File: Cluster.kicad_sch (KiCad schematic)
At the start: 26 parts, among them J1 DTM06-2S nickel, 12V input (s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, J2 SWD Tag-Connect, Q1 PMV37ENEA automotive (AEC-Q10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, U1 NXP S32K144 automotive (AEC-Q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, U2 LMR33630-Q1 (AEC-Q100 G1), U3 LM74700-Q1 (AEC-Q100 G1), U4 TLV733P-Q1 (AEC-Q100 G1), Y1 8MHz (AEC-Q200)

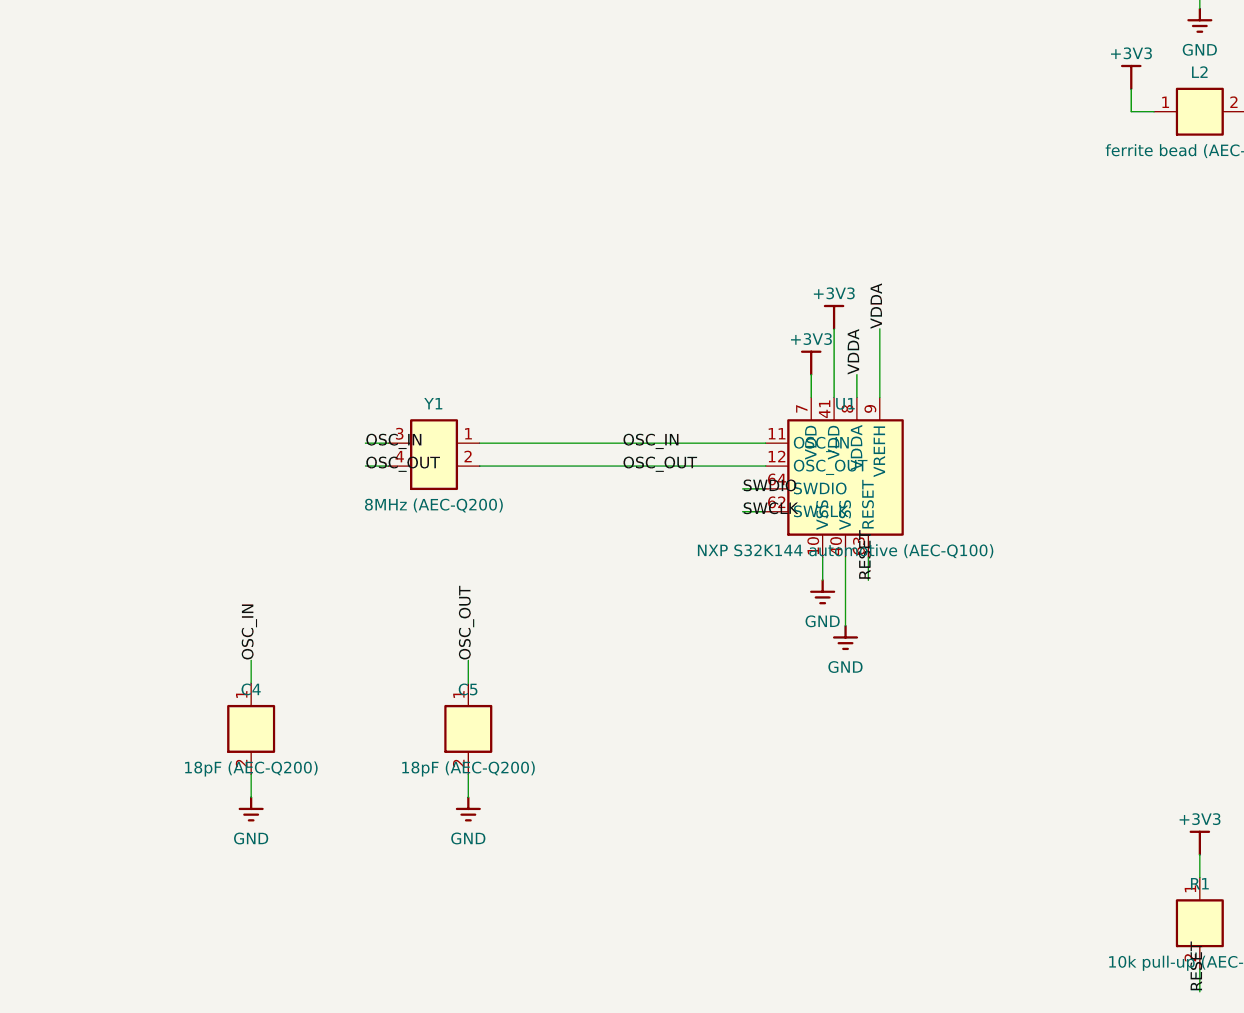
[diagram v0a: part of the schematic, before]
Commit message: Step 1: real S32K144 peripheral pin-mux for BT817AQ/aux gauges/CAN/ADC
Pulled the real IO signal table from NXP's own S32K1xx Reference Manual
(embedded xlsx attachment, extracted via pypdf) and picked 25
conflict-checked pins for LPSPI1 (BT817AQ QSPI), LPSPI2 (shared aux
gauge SPI bus), FlexCAN0, 4x ADC channel, and 9 plain GPIO. Wired as
real, named label stubs on U1 - not yet connected to any peripheral
chip, that's Steps 2-5. Regenerates clean; ERC shows only the expected
forward-stub findings.

Co-Authored-By: Claude Sonnet 5 <noreply@anthropic.com>
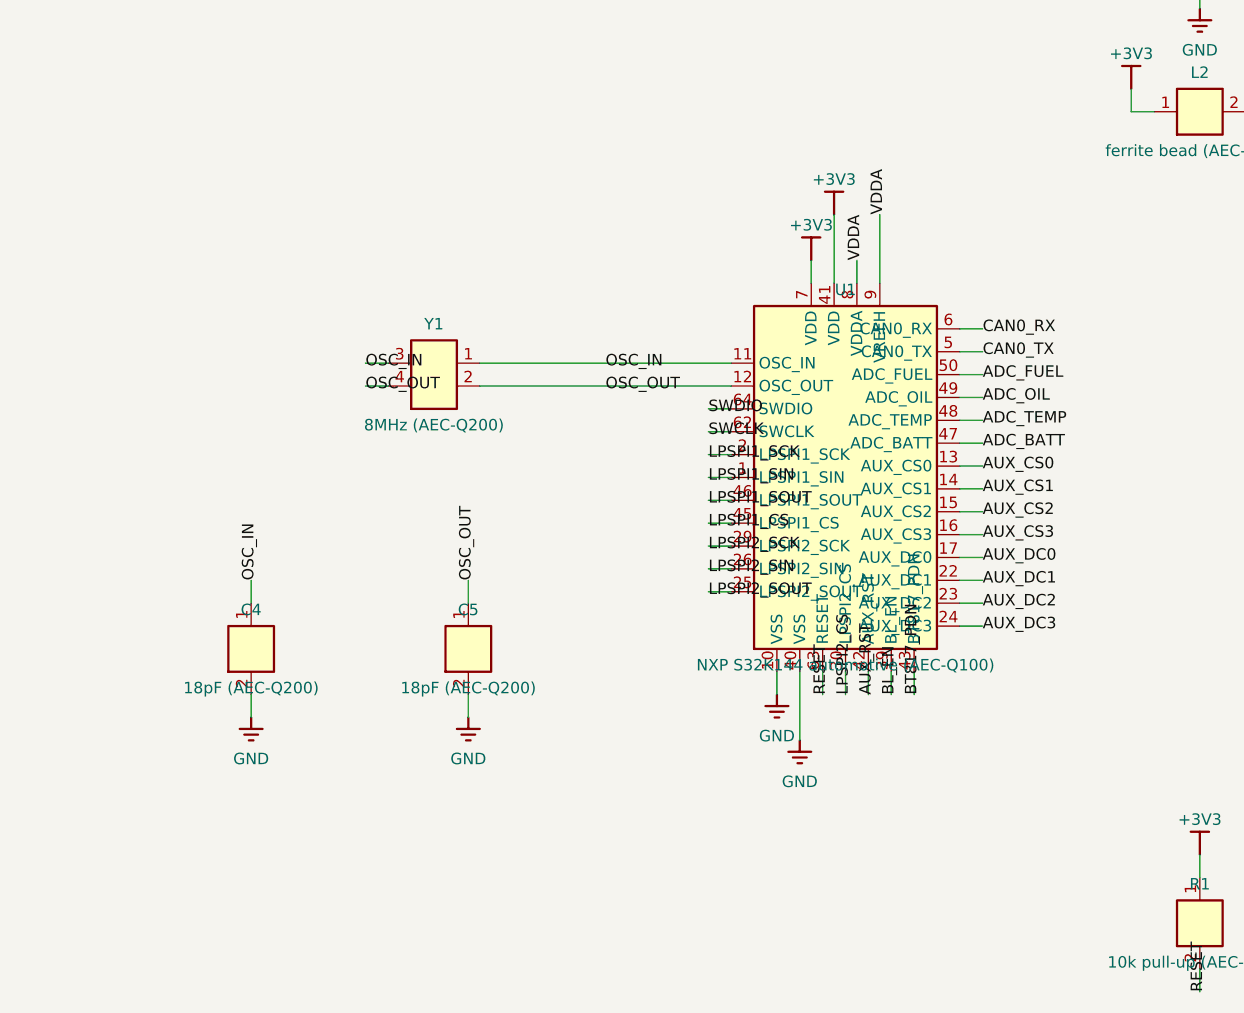
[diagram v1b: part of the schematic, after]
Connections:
- new net ADC_BATT: U1.47 (ADC_BATT)
- new net ADC_FUEL: U1.50 (ADC_FUEL)
- new net ADC_OIL: U1.49 (ADC_OIL)
- new net ADC_TEMP: U1.48 (ADC_TEMP)
- new net AUX_CS0: U1.13 (AUX_CS0)
- new net AUX_CS1: U1.14 (AUX_CS1)
- new net AUX_CS2: U1.15 (AUX_CS2)
- new net AUX_CS3: U1.16 (AUX_CS3)
- new net AUX_DC0: U1.17 (AUX_DC0)
- new net AUX_DC1: U1.22 (AUX_DC1)
- new net AUX_DC2: U1.23 (AUX_DC2)
- new net AUX_DC3: U1.24 (AUX_DC3)
- new net AUX_RST: U1.42 (AUX_RST)
- new net BL_EN: U1.39 (BL_EN)
- new net BT817_PDN: U1.43 (BT817_PDN)
- new net CAN0_RX: U1.6 (CAN0_RX)
- new net CAN0_TX: U1.5 (CAN0_TX)
- new net LPSPI1_CS: U1.45 (LPSPI1_CS)
- new net LPSPI1_SCK: U1.2 (LPSPI1_SCK)
- new net LPSPI1_SIN: U1.1 (LPSPI1_SIN)
- new net LPSPI1_SOUT: U1.46 (LPSPI1_SOUT)
- new net LPSPI2_CS: U1.30 (LPSPI2_CS)
- new net LPSPI2_SCK: U1.29 (LPSPI2_SCK)
- new net LPSPI2_SIN: U1.26 (LPSPI2_SIN)
- new net LPSPI2_SOUT: U1.25 (LPSPI2_SOUT)

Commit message: Steps 2-3: CAN0 transceiver + 4x GC9A01 aux gauges wired
Step 2: reused ecu-pcb's real, already-verified TJA1043T CAN transceiver
pin table and wiring topology verbatim (single CAN0 instance).

Step 3: registered the real 18-pin FPC table from Raystar's own
RFA401280B-AYW-DNF1 datasheet for the 4x GC9A01 aux gauges. Real finding
from reading the datasheet rather than assuming a generic GC9A01
breakout: backlight is a bare LED anode/cathode pair, not a logic-level
enable pin - wired with per-display series resistors from +5V and a
shared low-side MOSFET switch (reusing the power stage's own PMV37ENEA),
not 4 GPIO-driven logic pins.

Two real bugs caught and fixed by the script's own checks, not eyeballed:
a GND-riser-style collision between VCI3V3's power symbol and an
adjacent pin's stub, and a guessed FFC-FPC footprint name that doesn't
exist in KiCad's bundled library (fixed with a real bundled Amphenol
part). Grew the sheet from A2 to A1 for room. ERC clean except findings
that trace to Steps 4-5, not yet wired.

Co-Authored-By: Claude Sonnet 5 <noreply@anthropic.com>
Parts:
- added C13: 100nF VCC decouple (AEC-Q200), Capacitor_SMD:C_0603_1608Metric, symbol Cluster:C_V
- added C14: 100nF VIO decouple (AEC-Q200), Capacitor_SMD:C_0603_1608Metric, symbol Cluster:C_V
- added C15: 100nF VBAT decouple (AEC-Q200), Capacitor_SMD:C_0603_1608Metric, symbol Cluster:C_V
- added C16: 4.7nF SPLIT stabilization (AEC-Q200), Capacitor_SMD:C_0603_1608Metric, symbol Cluster:C_V
- added C17, C18, C19, C20: 100nF VCI decouple (AEC-Q200), Capacitor_SMD:C_0603_1608Metric, symbol Cluster:C_V
- added Q2: PMV37ENEA automotive (AEC-Q101) - shared aux-gaug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, Package_TO_SOT_SMD:SOT-23, symbol Cluster:MOSFET_N
- added R10: 100R BL_EN gate resistor (AEC-Q200), Resistor_SMD:R_0603_1608Metric, symbol Cluster:R_V
- added R11: 10k LPSPI2_SIN pull-down, idle-state definition (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, Resistor_SMD:R_0603_1608Metric, symbol Cluster:R_V
- added R4, R5: 60R split termination (AEC-Q200) - DNP unless bus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, Resistor_SMD:R_0603_1608Metric, symbol Cluster:R_V
- added R6, R7, R8, R9: 120R VLED series (self-calculated for ~15mA at 5V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, Resistor_SMD:R_0603_1608Metric, symbol Cluster:R_V
- added U5: NXP TJA1043T automotive CAN transceiver (AEC-Q100), Package_SO:SOIC-14_3.9x8.7mm_P1.27mm, symbol Cluster:TJA1043T
- added U6: Raystar RFA401280B-AYW-DNF1 - Fuel level gauge, Connector_FFC-FPC:Amphenol_F32Q-1A7x1-11018_1x18-1MP_P0.5mm_Horizontal, symbol Cluster:GC9A01_MODULE
- added U7: Raystar RFA401280B-AYW-DNF1 - Oil pressure gauge, Connector_FFC-FPC:Amphenol_F32Q-1A7x1-11018_1x18-1MP_P0.5mm_Horizontal, symbol Cluster:GC9A01_MODULE
- added U8: Raystar RFA401280B-AYW-DNF1 - Coolant temp gauge, Connector_FFC-FPC:Amphenol_F32Q-1A7x1-11018_1x18-1MP_P0.5mm_Horizontal, symbol Cluster:GC9A01_MODULE
- added U9: Raystar RFA401280B-AYW-DNF1 - Battery voltage gau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, Connector_FFC-FPC:Amphenol_F32Q-1A7x1-11018_1x18-1MP_P0.5mm_Horizontal, symbol Cluster:GC9A01_MODULE
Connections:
- net +3V3: now also C14.1, C17.1, C18.1, C19.1, C20.1, U5.5 (VIO), U6.16 (VCI3V3), U7.16 (VCI3V3), U8.16 (VCI3V3), U9.16 (VCI3V3)
- net +5V: now also C13.1, R6.1, R7.1, R8.1, R9.1, U5.3 (VCC)
- net AUX_CS0: now also U6.10 (CS)
- net AUX_CS1: now also U7.10 (CS)
- net AUX_CS2: now also U8.10 (CS)
- net AUX_CS3: now also U9.10 (CS)
- net AUX_DC0: now also U6.13 (RS)
- net AUX_DC1: now also U7.13 (RS)
- net AUX_DC2: now also U8.13 (RS)
- net AUX_DC3: now also U9.13 (RS)
- net AUX_RST: now also U6.15 (RESET), U7.15 (RESET), U8.15 (RESET), U9.15 (RESET)
- net BL_EN: now also R10.1
- net CAN0_RX: now also U5.4 (RXD)
- net CAN0_TX: now also U5.1 (TXD)
- net GND: now also C13.2, C14.2, C15.2, C16.2, C17.2, C18.2, C19.2, C20.2, Q2.3 (D), R11.2, U5.2 (GND), U5.9 (WAKE), U6.18 (GND), U6.5 (TP_GND), U6.9 (GND), U7.18 (GND), U7.5 (TP_GND), U7.9 (GND), U8.18 (GND), U8.5 (TP_GND), U8.9 (GND), U9.18 (GND), U9.5 (TP_GND), U9.9 (GND)
- net LPSPI2_SCK: now also U6.11 (SCL), U7.11 (SCL), U8.11 (SCL), U9.11 (SCL)
- net LPSPI2_SIN: now also R11.1
- net LPSPI2_SOUT: now also U6.12 (SDA), U7.12 (SDA), U8.12 (SDA), U9.12 (SDA)
- net VIN_PROT: now also C15.1, U5.10 (VBAT)
- net LPSPI2_CS: no longer names the net of U1.30 (LPSPI2_CS)
- new net AUX_VLED_RTN: Q2.2 (S), U6.8 (VLED-), U7.8 (VLED-), U8.8 (VLED-), U9.8 (VLED-)
- new net BL_GATE: Q2.1 (G), R10.2
- new net CAN0_EN: U1.18 (CAN0_EN), U5.6 (EN)
- new net CAN0_H: R4.1, U5.13 (CANH)
- new net CAN0_L: R5.2, U5.12 (CANL)
- new net CAN0_SPLIT: C16.1, R4.2, R5.1, U5.11 (SPLIT)
- new net CAN0_STB_N: U1.19 (CAN0_STB_N), U5.14 (STB_N)
- new net U6_VLED: R6.2, U6.7 (VLED+)
- new net U7_VLED: R7.2, U7.7 (VLED+)
- new net U8_VLED: R8.2, U8.7 (VLED+)
- new net U9_VLED: R9.2, U9.7 (VLED+)
- no-connect marks 3 -> 34
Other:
- note added: "4x GC9A01 AUX GAUGES: FUEL / OIL / COOLANT TEMP / BATTERY (PLAN STEP 3)"
- note added: "CAN0: NXP TJA1043T TRANSCEIVER (PLAN STEP 2)"

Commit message: Step 4: BT817AQ speedo co-processor + ST7701S module wired
Registered BT817AQ's real 64-pin VQFN table from Bridgetek's own
datasheet and the BH021WVC02 module's real 40-pin FPC table from
Panox's own datasheet. Real finding along the way: BT817A's VCC1V2
core rail is a genuine external 1.28V supply (not internally regulated
from VCC), so a new TPS7A16-Q1 adjustable LDO + FB divider was added,
sized from TI's own VREF spec. RGB666 wiring uses the module's own
documented bit order (DB0=Blue LSB..DB17=Red MSB) to map BT817AQ's
R7-R2/G7-G2/B7-B2 correctly. Speedo backlight reuses the same real
"series resistor + shared MOSFET switch" LED treatment as the aux
gauges, this time PWM-driven from BT817AQ's own BACKLIGHT output for
independent dimming.

Two real bugs caught and fixed, not eyeballed: a crystal-to-MCU wiring
attempt using wire_pins() across mismatched pin orientations (same
class of bug thermo-pcb's own history documents, fixed with label-based
connections instead), and a genuine placement collision between U10 and
Y2 that produced a real ERC pin_to_pin/multiple_net_names short -
confirmed via a rendered PDF crop showing the two symbols' pin fields
interleaved, fixed with real separation. ERC clean except findings that
trace to Step 5 (sensor ADC front end), not yet wired.

Co-Authored-By: Claude Sonnet 5 <noreply@anthropic.com>
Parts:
- added C21: 10uF IN cap (AEC-Q200), Capacitor_SMD:C_0603_1608Metric, symbol Cluster:C_V
- added C22: 10uF OUT cap, real min 2.2uF per TI's own stabili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, Capacitor_SMD:C_0603_1608Metric, symbol Cluster:C_V
- added C23, C24: 18pF (AEC-Q200), Capacitor_SMD:C_0603_1608Metric, symbol Cluster:C_V
- added C25: 100nF VCC decouple (AEC-Q200), Capacitor_SMD:C_0603_1608Metric, symbol Cluster:C_V
- added C26: 1uF VCC1V2 decouple (AEC-Q200), Capacitor_SMD:C_0603_1608Metric, symbol Cluster:C_V
- added C27: 100nF VCCIO decouple (AEC-Q200), Capacitor_SMD:C_0603_1608Metric, symbol Cluster:C_V
- added J3: Panox BH021WVC02 - center speedo, Connector_FFC-FPC:Amphenol_F32Q-1A7x1-11040_1x40-1MP_P0.5mm_Horizontal, symbol Cluster:ST7701S_MODULE
- added Q3: PMV37ENEA automotive (AEC-Q101) - speedo backligh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, Package_TO_SOT_SMD:SOT-23, symbol Cluster:MOSFET_N
- added R12: 7.32k FB divider top, self-calculated for 1.28V (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, Resistor_SMD:R_0603_1608Metric, symbol Cluster:R_V
- added R13: 100k FB divider bottom, self-calculated for 1.28V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, Resistor_SMD:R_0603_1608Metric, symbol Cluster:R_V
- added R14: 120R LEDA series (self-calculated, ~15mA at 5V - 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, Resistor_SMD:R_0603_1608Metric, symbol Cluster:R_V
- added R15: 100R SPD_BL_PWM gate resistor (AEC-Q200), Resistor_SMD:R_0603_1608Metric, symbol Cluster:R_V
- added U10: TPS7A16-Q1 (AEC-Q100 G1), Package_SO:Texas_DGN0008D_VSSOP-8-1EP_3x3mm_P0.65mm_EP2x2.94mm_Mask1.57x1.89mm, symbol Cluster:IC_LDO_ADJ
- added U11: Bridgetek BT817AQ automotive (AEC-Q100 G2), Package_DFN_QFN:QFN-64-1EP_9x9mm_P0.5mm_EP4.1x4.1mm, symbol Cluster:BT817AQ
- added Y2: 12MHz (AEC-Q200), Crystal:Crystal_SMD_3225-4Pin_3.2x2.5mm, symbol Cluster:XTAL_BT817
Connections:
- net +3V3: now also C21.1, C25.1, C27.1, J3.5 (VCI), U10.5 (EN), U10.8 (IN), U11.17 (VCCIO3), U11.24 (VCC), U11.27 (VCCA), U11.28 (VCCIO2), U11.9 (VCCIO1)
- net +5V: now also R14.1
- net BT817_PDN: now also U11.12 (PD_N)
- net GND: now also C21.2, C22.2, C23.2, C24.2, C25.2, C26.2, C27.2, J3.34 (GND), J3.4 (GND), J3.40 (GND), Q3.3 (D), R13.2, U10.4 (GND), U10.9 (EP), U11.18 (SPIM_MISO), U11.23 (GND), U11.33 (GND), U11.48 (GND), U11.65 (EP)
- net LPSPI1_CS: now also U11.6 (CS_N)
- net LPSPI1_SCK: now also U11.3 (SCK)
- net LPSPI1_SIN: now also U11.4 (MISO)
- net LPSPI1_SOUT: now also U11.5 (MOSI)
- new net BT817_X1: C23.1, U11.21 (X1), Y2.1 (X1), Y2.3 (X1)
- new net BT817_X2: C24.1, U11.22 (X2), Y2.2 (X2), Y2.4 (X2)
- new net DE: J3.13 (DE), U11.35 (DE)
- new net FB1V2: R12.2, R13.1, U10.2 (FB)
- new net HSYNC: J3.15 (HSYNC), U11.37 (HSYNC)
- new net J3_LEDA: J3.1 (LEDA), R14.2
- new net PCLK: J3.12 (PCLK), U11.39 (PCLK)
- new net SPD_B2: J3.16 (DB0), U11.45 (B2)
- new net SPD_B3: J3.17 (DB1), U11.44 (B3)
- new net SPD_B4: J3.18 (DB2), U11.43 (B4)
- new net SPD_B5: J3.19 (DB3), U11.42 (B5)
- new net SPD_B6: J3.20 (DB4), U11.41 (B6)
- new net SPD_B7: J3.21 (DB5), U11.40 (B7)
- new net SPD_BL_GATE: Q3.1 (G), R15.2
- new net SPD_BL_PWM: R15.1, U11.34 (BACKLIGHT)
- new net SPD_G2: J3.22 (DB6), U11.54 (G2)
- new net SPD_G3: J3.23 (DB7), U11.53 (G3)
- new net SPD_G4: J3.24 (DB8), U11.52 (G4)
- new net SPD_G5: J3.25 (DB9), U11.51 (G5)
- new net SPD_G6: J3.26 (DB10), U11.50 (G6)
- new net SPD_G7: J3.27 (DB11), U11.49 (G7)
- new net SPD_R2: J3.28 (DB12), U11.63 (R2)
- new net SPD_R3: J3.29 (DB13), U11.62 (R3)
- new net SPD_R4: J3.30 (DB14), U11.61 (R4)
- new net SPD_R5: J3.31 (DB15), U11.60 (R5)
- new net SPD_R6: J3.32 (DB16), U11.59 (R6)
- new net SPD_R7: J3.33 (DB17), U11.58 (R7)
- new net SPD_VLED_RTN: J3.2 (LEDK), J3.3 (LEDK), Q3.2 (S)
- new net ST7701_CS: J3.11 (CS), U11.10 (GPIO2)
- new net ST7701_RESET: J3.6 (RESET), U11.13 (GPIO3)
- new net ST7701_SCK: J3.10 (SCK), U11.8 (GPIO1)
- new net ST7701_SDA: J3.9 (SDA), U11.7 (GPIO0)
- new net VCC1V2: C22.1, C26.1, R12.1, U10.1 (OUT), U11.2 (VCC1V2), U11.25 (VCC1V2), U11.57 (VCC1V2)
- new net VSYNC: J3.14 (VSYNC), U11.36 (VSYNC)
- no-connect marks 34 -> 62
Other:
- note added: "BT817AQ + ST7701S SPEEDO MODULE (PLAN STEP 4)"

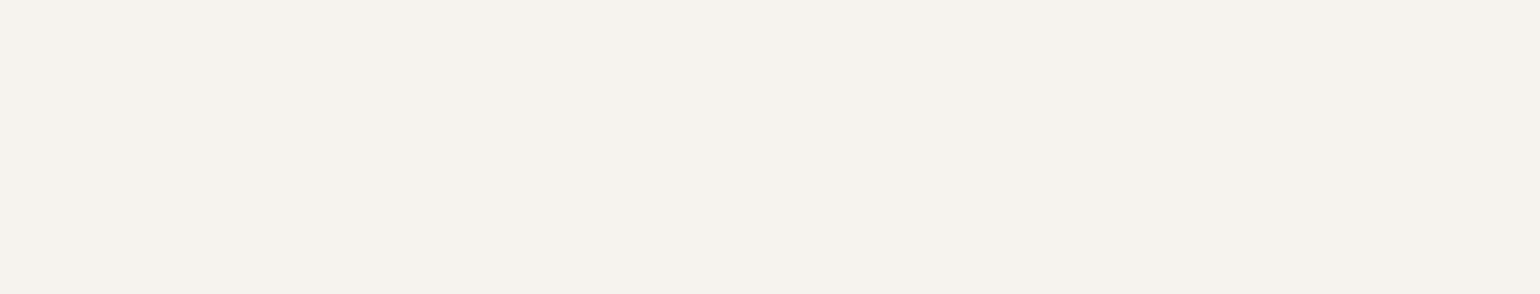
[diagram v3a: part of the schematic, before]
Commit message: Step 5: sensor ADC front end wired; schematic now fully wired
Fuel/oil/temp resistive dividers sized per-sender from the real
published curves (fuel/oil share a 47R pull-up given their similar
10-70ish-ohm range; coolant temp gets its own 100R pull-up for its much
wider 10-300R range). Battery voltage divider (49.9k/10k) scaled for
the real 9-16V automotive range with margin below the ADC's 3.3V rail.

ERC is down to exactly the 4 baseline findings every sibling board's
finished schematic carries (VDDA/U2-VIN/+5V power_pin_not_driven,
SWCLK driven off-sheet) - every real forward stub from Steps 1-5 is now
resolved except the genuine off-board harness connections pending Step
6. Also grew the sheet A1->A0: a full-page render (the same "always
verify with a real render" discipline this family's history keeps
re-learning) showed J3 genuinely clipped past A1's right edge.

Co-Authored-By: Claude Sonnet 5 <noreply@anthropic.com>
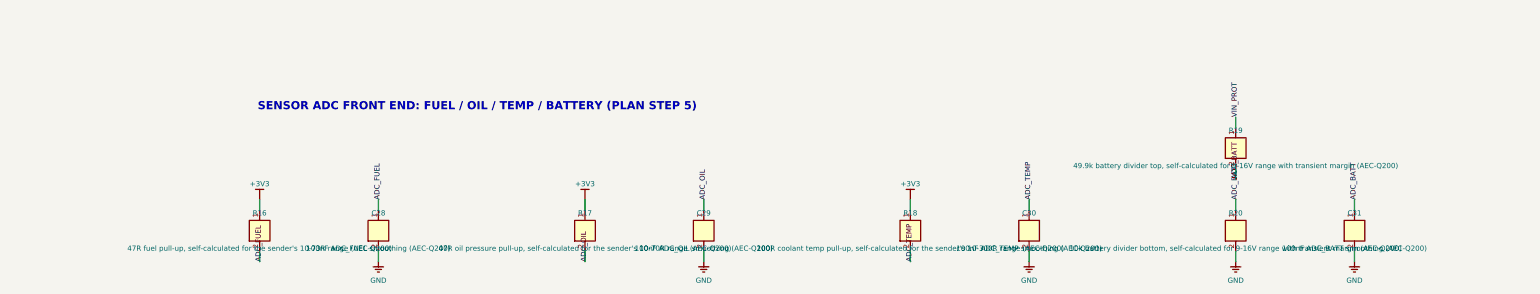
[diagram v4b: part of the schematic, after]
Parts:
- added C28: 100nF ADC_FUEL smoothing (AEC-Q200), Capacitor_SMD:C_0603_1608Metric, symbol Cluster:C_V
- added C29: 100nF ADC_OIL smoothing (AEC-Q200), Capacitor_SMD:C_0603_1608Metric, symbol Cluster:C_V
- added C30: 100nF ADC_TEMP smoothing (AEC-Q200), Capacitor_SMD:C_0603_1608Metric, symbol Cluster:C_V
- added C31: 100nF ADC_BATT smoothing (AEC-Q200), Capacitor_SMD:C_0603_1608Metric, symbol Cluster:C_V
- added R16: 47R fuel pull-up, self-calculated for the sender'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, Resistor_SMD:R_0603_1608Metric, symbol Cluster:R_V
- added R17: 47R oil pressure pull-up, self-calculated for the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, Resistor_SMD:R_0603_1608Metric, symbol Cluster:R_V
- added R18: 100R coolant temp pull-up, self-calculated for th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, Resistor_SMD:R_0603_1608Metric, symbol Cluster:R_V
- added R19: 49.9k battery divider top, self-calculated for 9-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, Resistor_SMD:R_0603_1608Metric, symbol Cluster:R_V
- added R20: 10k battery divider bottom, self-calculated for 9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, Resistor_SMD:R_0603_1608Metric, symbol Cluster:R_V
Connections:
- net +3V3: now also R16.1, R17.1, R18.1
- net ADC_BATT: now also C31.1, R19.2, R20.1
- net ADC_FUEL: now also C28.1, R16.2
- net ADC_OIL: now also C29.1, R17.2
- net ADC_TEMP: now also C30.1, R18.2
- net GND: now also C28.2, C29.2, C30.2, C31.2, R20.2
- net VIN_PROT: now also R19.1
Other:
- note added: "SENSOR ADC FRONT END: FUEL / OIL / TEMP / BATTERY (PLAN STEP 5)"
